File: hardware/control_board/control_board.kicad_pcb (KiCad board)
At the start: 2 copper layers, 60 x 40 mm, 4 parts

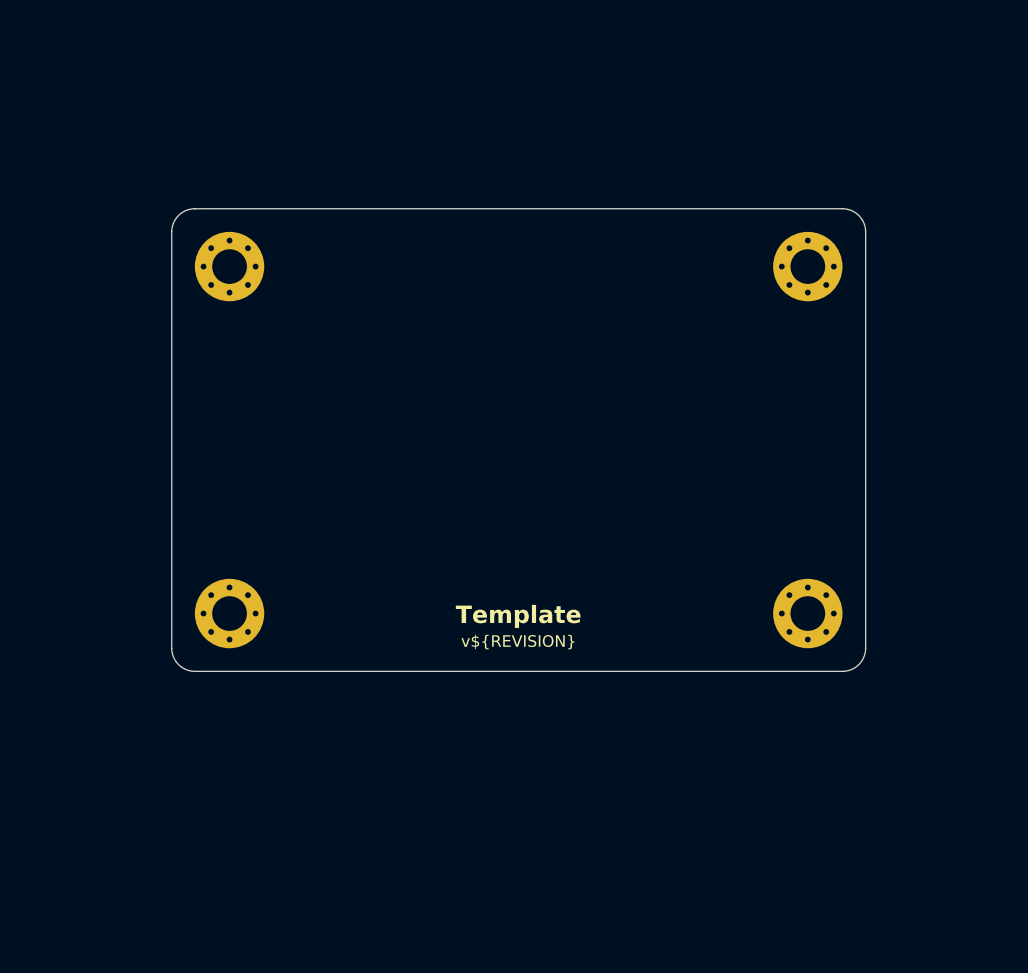
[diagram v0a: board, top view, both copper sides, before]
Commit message: Place components on the control board PCB
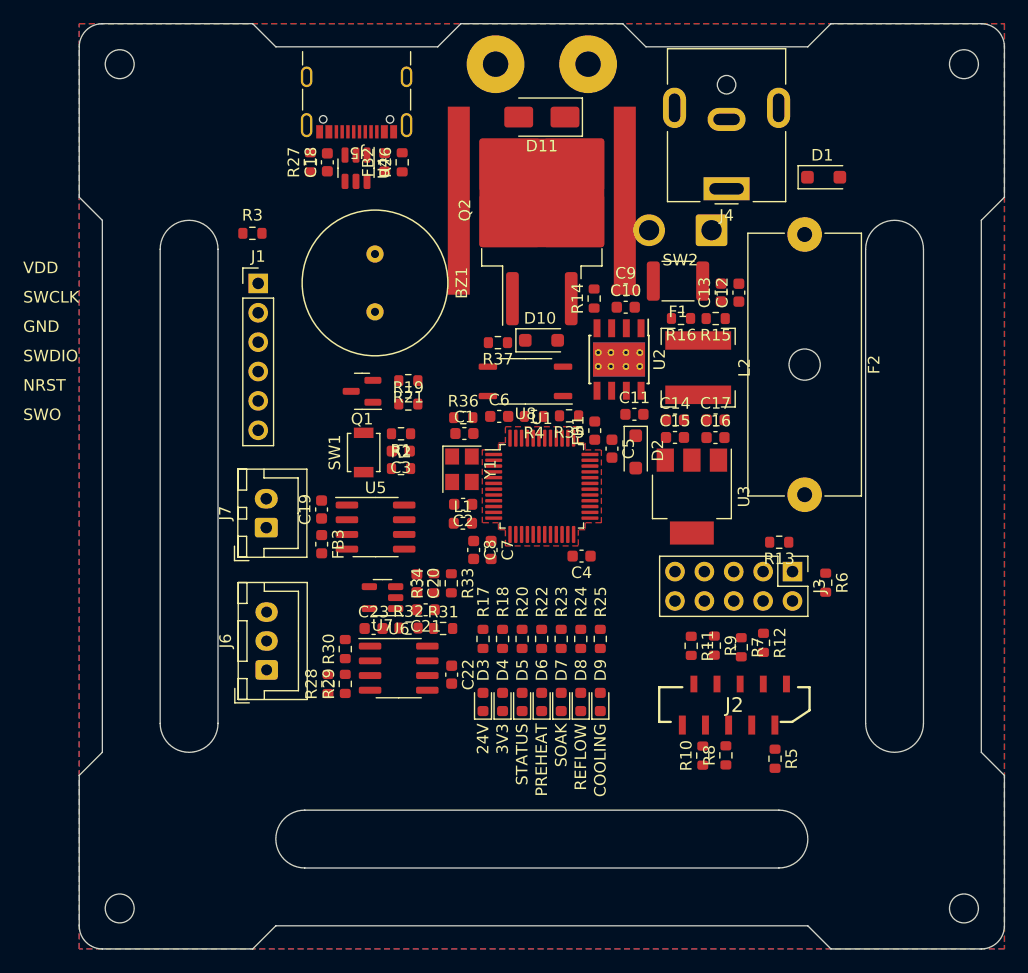
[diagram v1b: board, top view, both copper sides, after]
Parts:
- removed REF** (x4): MountingHole_3mm_Pad_Via, MountingHole:MountingHole_3mm_Pad_Via
- added BZ1: Buzzer, Local_Library:PKM13EPYH4000-A0, F.Cu at (133.6, 82.4)
- added C1: 10p, Capacitor_SMD:C_0603_1608Metric, F.Cu at (141.3, 95.4)
- added C10: 100n, Capacitor_SMD:C_0603_1608Metric, F.Cu at (155.3, 84.5)
- added C11: 100n, Capacitor_SMD:C_0603_1608Metric, F.Cu at (156.0, 93.8)
- added C12: 22u, Capacitor_SMD:C_0603_1608Metric, F.Cu at (165.0, 83.3)
- added C13: 22u, Capacitor_SMD:C_0603_1608Metric, F.Cu at (163.5, 83.2)
- added C14: 1u, Capacitor_SMD:C_0603_1608Metric, F.Cu at (159.5, 94.3)
- added C15: 100n, Capacitor_SMD:C_0603_1608Metric, F.Cu at (159.5, 95.8)
- added C16: 100n, Capacitor_SMD:C_0603_1608Metric, F.Cu at (163.0, 95.8)
- added C17: 1u, Capacitor_SMD:C_0603_1608Metric, F.Cu at (163.0, 94.3)
- added C18: 100n, Capacitor_SMD:C_0603_1608Metric, F.Cu at (129.5, 72.0)
- added C19: 100n, Capacitor_SMD:C_0603_1608Metric, F.Cu at (129.0, 102.0)
- added C2: 10p, Capacitor_SMD:C_0603_1608Metric, F.Cu at (141.2, 101.6)
- added C20: 100n, Capacitor_SMD:C_0603_1608Metric, F.Cu at (137.2, 108.4)
- added C21: 100n, Capacitor_SMD:C_0603_1608Metric, F.Cu at (138.0, 110.7)
- added C22: 100n, Capacitor_SMD:C_0603_1608Metric, F.Cu at (140.2, 116.3)
- added C23: 100n, Capacitor_SMD:C_0603_1608Metric, F.Cu at (133.5, 112.3)
- added C3: 100n, Capacitor_SMD:C_0603_1608Metric, F.Cu at (135.8, 97.0)
- added C4: 100n, Capacitor_SMD:C_0603_1608Metric, F.Cu at (151.4, 106.0)
- added C5: 100n, Capacitor_SMD:C_0603_1608Metric, F.Cu at (154.1, 96.7)
- added C6: 100n, Capacitor_SMD:C_0603_1608Metric, F.Cu at (144.3, 94.0)
- added C7: 1u, Capacitor_SMD:C_0603_1608Metric, F.Cu at (143.6, 105.5)
- added C8: 100n, Capacitor_SMD:C_0603_1608Metric, F.Cu at (142.1, 105.5)
- added C9: 4u7, Capacitor_SMD:C_0603_1608Metric, F.Cu at (155.3, 83.0)
- added D1: MBR1020VL, Diode_SMD:D_SOD-123F, F.Cu at (172.4, 73.3)
- added D10: 15V, Diode_SMD:D_SOD-123F, F.Cu at (148.0, 87.4)
- added D11: SK36A, Diode_SMD:D_SMA, F.Cu at (148.0, 68.1)
- added D2: 5V6, Diode_SMD:D_SOD-123F, F.Cu at (156.1, 97.0)
- added D3: Green, LED_SMD:LED_0603_1608Metric, F.Cu at (142.9, 118.6)
- added D4: Green, LED_SMD:LED_0603_1608Metric, F.Cu at (144.6, 118.6)
- added D5: Yellow, LED_SMD:LED_0603_1608Metric, F.Cu at (146.3, 118.6)
- added D6: Yellow, LED_SMD:LED_0603_1608Metric, F.Cu at (148.0, 118.6)
- added D7: Yellow, LED_SMD:LED_0603_1608Metric, F.Cu at (149.7, 118.6)
- added D8: Yellow, LED_SMD:LED_0603_1608Metric, F.Cu at (151.4, 118.6)
- added D9: Yellow, LED_SMD:LED_0603_1608Metric, F.Cu at (153.1, 118.6)
- added F1: 500mA, Local_Library:MINISMDCx, F.Cu at (159.8, 82.3)
- added F2: 10A, Fuse:Fuseholder_Cylinder-5x20mm_Schurter_0031_8201_Horizontal_Open, F.Cu at (170.7, 78.2)
- added FB1: 600R@100MHz, Inductor_SMD:L_0603_1608Metric, F.Cu at (152.6, 95.2)
- added FB2: 600R@100MHz, Inductor_SMD:L_0603_1608Metric, F.Cu at (134.4, 72.0)
- added FB3: 600R@100MHz, Inductor_SMD:L_0603_1608Metric, F.Cu at (129.0, 105.0)
- added G***: LOGO, Local_Library:PUTM_BOX_15MM, B.Cu at (148.0, 103.0)
- added G***: LOGO, Local_Library:QRCodeFrame_10mm, B.Cu at (148.0, 115.0)
- added H1: 2.5mm, MountingHole:MountingHole_2.5mm, F.Cu at (184.5, 63.5)
- added H2: 2.5mm, MountingHole:MountingHole_2.5mm, F.Cu at (111.5, 63.5)
- added H3: 2.5mm, MountingHole:MountingHole_2.5mm, F.Cu at (111.5, 136.5)
- added H4: 2.5mm, MountingHole:MountingHole_2.5mm, F.Cu at (184.5, 136.5)
- added HS1: 217-36CTE6, Local_Library:217-36CTx6, F.Cu at (148.0, 75.3)
- added J1: SWD, Connector_PinHeader_2.54mm:PinHeader_1x06_P2.54mm_Vertical, F.Cu at (123.5, 82.5)
- added J2: Panel, Local_Library:52808-1070, F.Cu at (164.7, 118.9)
- added J3: Aux, Connector_PinHeader_2.54mm:PinHeader_2x05_P2.54mm_Vertical, F.Cu at (169.7, 107.4)
- added J4: 6.5/2mm, Connector_BarrelJack:BarrelJack_CUI_PJ-063AH_Horizontal, F.Cu at (164.0, 74.3)
- added J5: USB_C, Connector_USB:USB_C_Receptacle_GCT_USB4105-xx-A_16P_TopMnt_Horizontal, F.Cu at (132.0, 65.7)
- added J6: RTD, Connector_JST:JST_XH_B3B-XH-A_1x03_P2.50mm_Vertical, F.Cu at (124.2, 115.9)
- added J7: TC, Connector_JST:JST_XH_B2B-XH-A_1x02_P2.50mm_Vertical, F.Cu at (124.2, 103.6)
- added J8: Conn_01x01, Local_Library:Pad_D5mm_H2.2mm, F.Cu at (152.0, 63.5)
- added J9: Conn_01x01, Local_Library:Pad_D5mm_H2.2mm, F.Cu at (144.0, 63.5)
- added L1: 10u, Inductor_SMD:L_0603_1608Metric, F.Cu at (141.2, 103.2)
- added L2: 15u, Local_Library:SRN6028Cx, F.Cu at (161.5, 89.7)
- added Q1: 2N7002A, Package_TO_SOT_SMD:SOT-23, F.Cu at (132.5, 91.8)
- added Q2: IRF1018ESTRLPBF, Package_TO_SOT_SMD:TO-263-2, F.Cu at (148.0, 76.1)
- added R1: 1k, Resistor_SMD:R_0603_1608Metric, F.Cu at (135.8, 95.5)
- added R10: 100R, Resistor_SMD:R_0603_1608Metric, F.Cu at (161.9, 123.3)
- added R11: 100R, Resistor_SMD:R_0603_1608Metric, F.Cu at (160.9, 113.8)
- added R12: 10k, Resistor_SMD:R_0603_1608Metric, F.Cu at (167.2, 113.5)
- added R13: 10k, Resistor_SMD:R_0603_1608Metric, F.Cu at (168.5, 104.8)
- added R14: 25k5, Resistor_SMD:R_0603_1608Metric, F.Cu at (152.5, 83.8)
- added R15: 100k, Resistor_SMD:R_0603_1608Metric, F.Cu at (163.0, 85.5)
- added R16: 24k9, Resistor_SMD:R_0603_1608Metric, F.Cu at (160.0, 85.5)
- added R17: 2k2, Resistor_SMD:R_0603_1608Metric, F.Cu at (142.9, 113.2)
- added R18: 120R, Resistor_SMD:R_0603_1608Metric, F.Cu at (144.6, 113.2)
- added R19: 100R, Resistor_SMD:R_0603_1608Metric, F.Cu at (136.5, 92.9)
- added R2: 10k, Resistor_SMD:R_0603_1608Metric, F.Cu at (135.8, 98.5)
- added R20: 120R, Resistor_SMD:R_0603_1608Metric, F.Cu at (146.3, 113.2)
- added R21: 10k, Resistor_SMD:R_0603_1608Metric, F.Cu at (136.5, 90.9)
- added R22: 120R, Resistor_SMD:R_0603_1608Metric, F.Cu at (148.0, 113.2)
- added R23: 120R, Resistor_SMD:R_0603_1608Metric, F.Cu at (149.7, 113.2)
- added R24: 120R, Resistor_SMD:R_0603_1608Metric, F.Cu at (151.4, 113.2)
- added R25: 120R, Resistor_SMD:R_0603_1608Metric, F.Cu at (153.1, 113.2)
- added R26: 5k1, Resistor_SMD:R_0603_1608Metric, F.Cu at (135.9, 72.0)
- added R27: 5k1, Resistor_SMD:R_0603_1608Metric, F.Cu at (128.0, 72.0)
- added R28: 1k, Resistor_SMD:R_0603_1608Metric, F.Cu at (129.5, 117.1)
- added R29: 1k, Resistor_SMD:R_0603_1608Metric, F.Cu at (131.0, 117.1)
- added R3: 0R, Resistor_SMD:R_0603_1608Metric, F.Cu at (123.0, 78.1)
- added R30: 100R, Resistor_SMD:R_0603_1608Metric, F.Cu at (131.0, 114.1)
- added R31: 5k, Resistor_SMD:R_0603_1608Metric, F.Cu at (139.5, 112.3)
- added R32: 1k, Resistor_SMD:R_0603_1608Metric, F.Cu at (136.5, 112.3)
- added R33: 3k3, Resistor_SMD:R_0603_1608Metric, F.Cu at (140.2, 108.4)
- added R34: 3k3, Resistor_SMD:R_0603_1608Metric, F.Cu at (138.7, 108.4)
- added R35: 100R, Resistor_SMD:R_0603_1608Metric, F.Cu at (150.4, 93.9)
- added R36: 1k, Resistor_SMD:R_0603_1608Metric, F.Cu at (141.2, 94.1)
- added R37: 1k, Resistor_SMD:R_0603_1608Metric, F.Cu at (144.2, 87.6)
- added R4: 10k, Resistor_SMD:R_0603_1608Metric, F.Cu at (147.3, 94.0)
- added R5: 10k, Resistor_SMD:R_0603_1608Metric, F.Cu at (168.2, 123.6)
- added R6: 10k, Resistor_SMD:R_0603_1608Metric, F.Cu at (172.5, 108.3)
- added R7: 270R, Resistor_SMD:R_0603_1608Metric, F.Cu at (165.2, 113.9)
- added R8: 100R, Resistor_SMD:R_0603_1608Metric, F.Cu at (163.9, 123.3)
- added R9: 100R, Resistor_SMD:R_0603_1608Metric, F.Cu at (162.9, 113.8)
- added SW1: Reset, Button_Switch_SMD:SW_SPST_B3U-1000P, F.Cu at (132.6, 97.1)
- added SW2: Power, Connector_Wire:SolderWire-1sqmm_1x02_P5.4mm_D1.4mm_OD2.7mm, F.Cu at (162.7, 77.9)
- added U1: STM32F103C8T6, Package_QFP:LQFP-48_7x7mm_P0.5mm, F.Cu at (148.0, 100.0)
- added U2: LMR38010SDDAR, Package_SO:TI_SO-PowerPAD-8_ThermalVias, F.Cu at (154.7, 89.0)
- added U3: TLV76133DCYR, Package_TO_SOT_SMD:SOT-223-3_TabPin2, F.Cu at (161.0, 100.9)
- added U4: USBLC6-2SC6, Package_TO_SOT_SMD:SOT-23-6, F.Cu at (131.9, 72.5)
- added U5: MAX6675, Package_SO:SOIC-8_3.9x4.9mm_P1.27mm, F.Cu at (133.6, 103.5)
- added U6: MCP6N11T-005E, Package_SO:SOIC-8_3.9x4.9mm_P1.27mm, F.Cu at (135.6, 115.7)
- added U7: MCP6001T, Package_TO_SOT_SMD:SOT-23-5, F.Cu at (134.2, 109.6)
- added U8: TLP183, Package_SO:SOIC-4_4.55x3.7mm_P2.54mm, F.Cu at (146.6, 90.9)
- added Y1: 8MHz, Crystal:Crystal_SMD_3225-4Pin_3.2x2.5mm, F.Cu at (141.1, 98.5)
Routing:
- added copper zone on B.Cu, net GND
- added copper zone on F.Cu, net GND
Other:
- board size 60 x 40 mm -> 80 x 80 mm
- board text added: "2023-08-06"
- board text added: "24V"
- board text added: "3V3"
- board text added: "Author: I. Kajdan"
- board text added: "COOLING"
- board text added: "GND"
- board text added: "JLCJLCJLCJLC"
- board text added: "NRST"
- board text added: "PREHEAT"
- board text added: "Promoter: A. Bondyra, Ph.D."
- board text added: "REFLOW"
- board text added: "Reflow Hot Plate"
- board text added: "SOAK"
- board text added: "STATUS"
- board text added: "SWCLK"
- board text added: "SWDIO"
- board text added: "SWO"
- board text added: "VDD"
- board text removed: "Template"

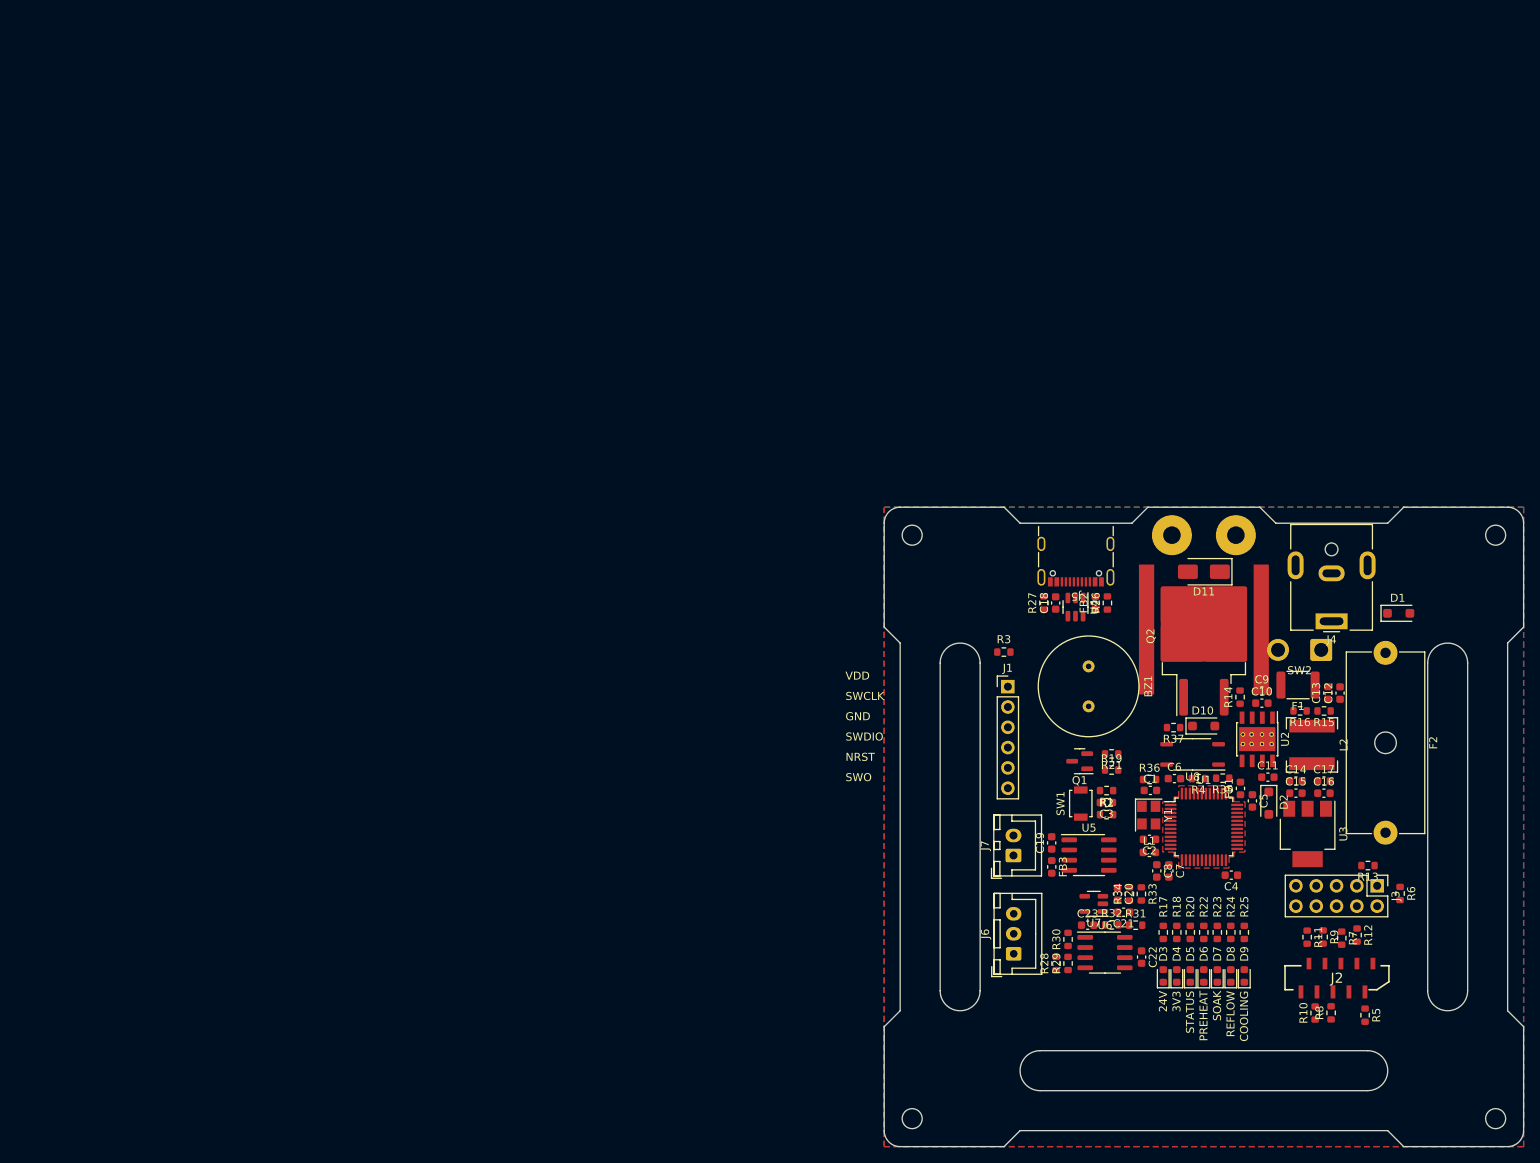
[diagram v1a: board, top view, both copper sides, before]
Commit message: Route front panel PCB tracks
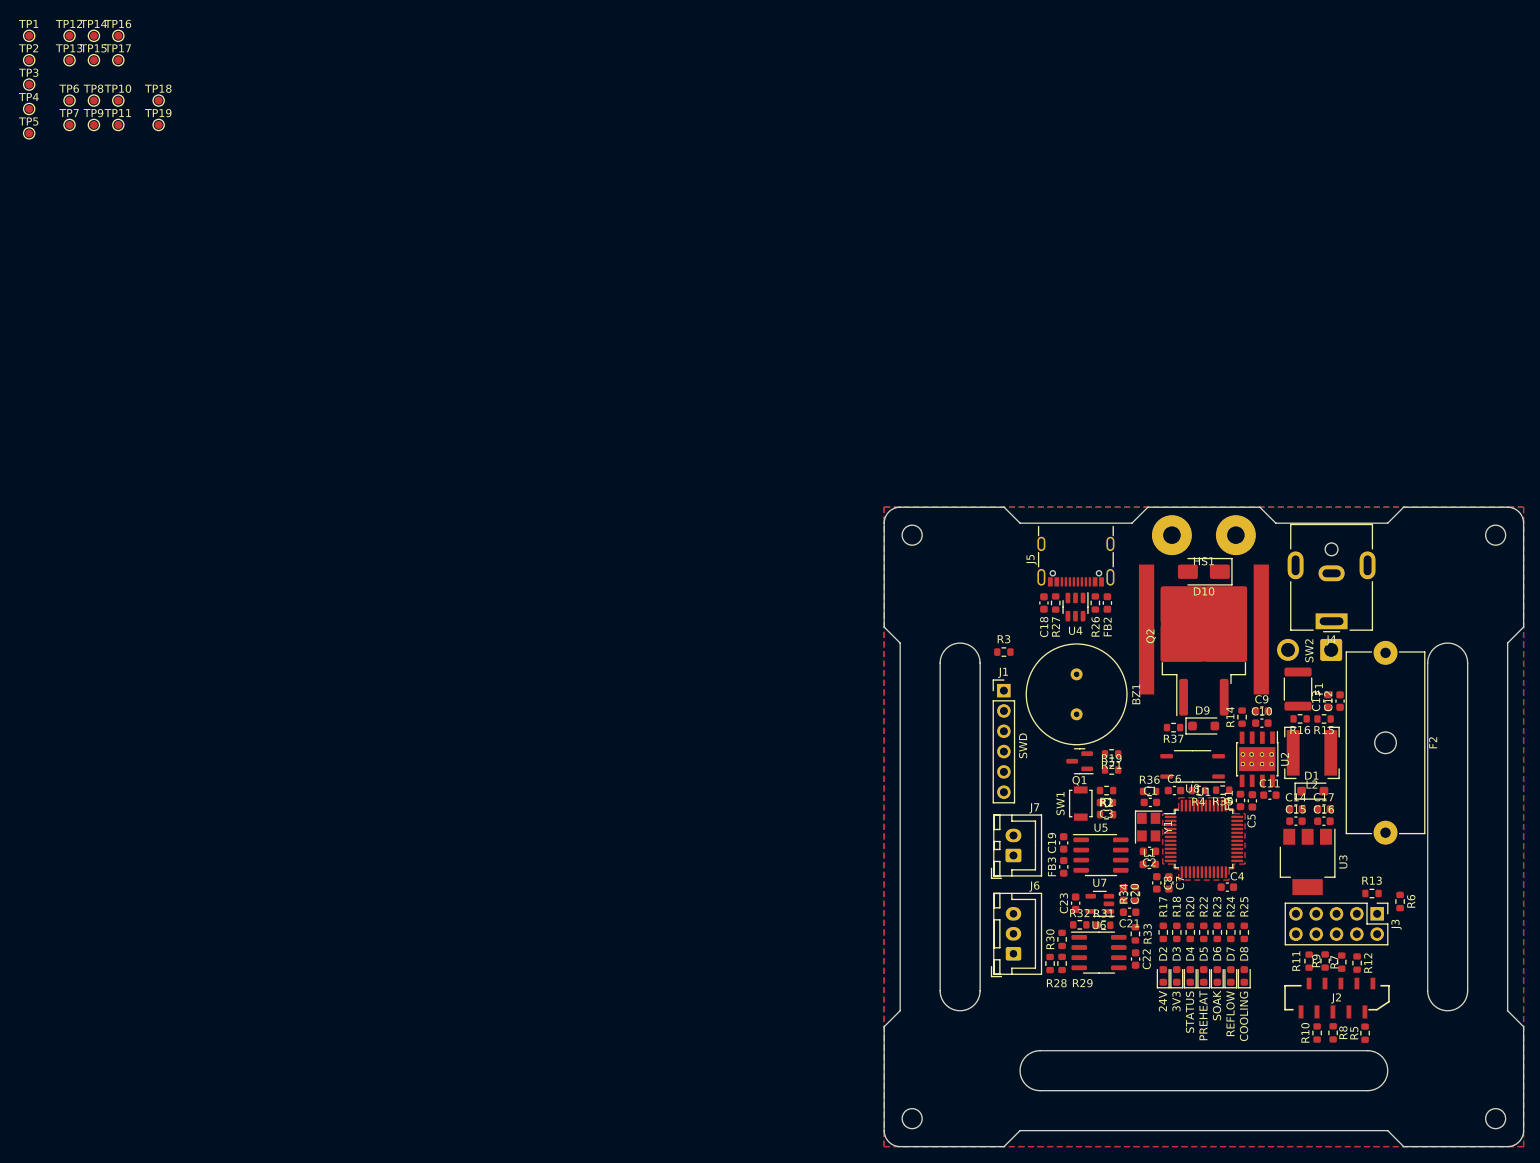
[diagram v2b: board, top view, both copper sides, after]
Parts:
- removed the D1 at (172.4, 73.3)
- added TP1: TestPoint_Small, TestPoint:TestPoint_Pad_D1.0mm, F.Cu at (1.02, 1.02)
- added TP10: TestPoint_Small, TestPoint:TestPoint_Pad_D1.0mm, F.Cu at (12.2, 9.12)
- added TP11: TestPoint_Small, TestPoint:TestPoint_Pad_D1.0mm, F.Cu at (12.2, 12.2)
- added TP12: TestPoint_Small, TestPoint:TestPoint_Pad_D1.0mm, F.Cu at (6.08, 1.02)
- added TP13: TestPoint_Small, TestPoint:TestPoint_Pad_D1.0mm, F.Cu at (6.08, 4.08)
- added TP14: TestPoint_Small, TestPoint:TestPoint_Pad_D1.0mm, F.Cu at (9.12, 1.02)
- added TP15: TestPoint_Small, TestPoint:TestPoint_Pad_D1.0mm, F.Cu at (9.12, 4.08)
- added TP16: TestPoint_Small, TestPoint:TestPoint_Pad_D1.0mm, F.Cu at (12.2, 1.02)
- added TP17: TestPoint_Small, TestPoint:TestPoint_Pad_D1.0mm, F.Cu at (12.2, 4.08)
- added TP18: TestPoint_Small, TestPoint:TestPoint_Pad_D1.0mm, F.Cu at (17.2, 9.12)
- added TP19: TestPoint_Small, TestPoint:TestPoint_Pad_D1.0mm, F.Cu at (17.2, 12.2)
- added TP2: TestPoint_Alt, TestPoint:TestPoint_Pad_D1.0mm, F.Cu at (1.02, 4.08)
- added TP3: TestPoint_Small, TestPoint:TestPoint_Pad_D1.0mm, F.Cu at (1.02, 7.12)
- added TP4: TestPoint_Small, TestPoint:TestPoint_Pad_D1.0mm, F.Cu at (1.02, 10.2)
- added TP5: TestPoint_Small, TestPoint:TestPoint_Pad_D1.0mm, F.Cu at (1.02, 13.2)
- added TP6: TestPoint_Small, TestPoint:TestPoint_Pad_D1.0mm, F.Cu at (6.08, 9.12)
- added TP7: TestPoint_Small, TestPoint:TestPoint_Pad_D1.0mm, F.Cu at (6.08, 12.2)
- added TP8: TestPoint_Small, TestPoint:TestPoint_Pad_D1.0mm, F.Cu at (9.12, 9.12)
- added TP9: TestPoint_Small, TestPoint:TestPoint_Pad_D1.0mm, F.Cu at (9.12, 12.2)
- moved D1 5.70 mm to (161.6, 95.5), turned to 0 degrees
- moved R33 5.06 mm to (139.4, 113.4), turned to 90 degrees
- moved R31 4.00 mm to (135.5, 112.3)
- moved R32 4.00 mm to (132.5, 112.3)
- moved R13 3.54 mm to (169.0, 108.3)
- moved C14 3.50 mm to (159.5, 97.8)
- moved C15 3.50 mm to (159.5, 99.3)
- moved C16 3.50 mm to (163.0, 99.3)
- moved C17 3.50 mm to (163.0, 97.8)
- moved J3 3.50 mm to (169.7, 110.9)
- moved R12 3.50 mm to (167.2, 117.0)
- moved U3 3.50 mm to (161.0, 104.4)
- moved C23 3.13 mm to (132.0, 109.5), turned to 90 degrees
- moved R11 3.01 mm to (161.2, 116.8)
- moved R9 3.01 mm to (163.2, 116.8)
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- renumbered D2 to D1, D11 to D10, D3 to D2, D4 to D3, D5 to D4, D6 to D5, D7 to D6, D8 to D7, D9 to D8, D10 to D9
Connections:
- C12 pad 1: /Power Supply/VOUT -> +5V
- C13 pad 1: /Power Supply/VOUT -> +5V
- HS1 pad 2: (no net) -> unconnected-(HS1-Pad2)
- L2 pad 2: /Power Supply/VOUT -> +5V
- R15 pad 1: /Power Supply/VOUT -> +5V
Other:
- board text added: "+"
- board text added: "-"
- board text added: "CLK"
- board text added: "DIO"
- board text added: "OUT"
- board text added: "RST"
- board text added: "SWD"
- board text removed: "NRST"
- board text removed: "SWCLK"
- board text removed: "SWDIO"
- board text removed: "SWO"
